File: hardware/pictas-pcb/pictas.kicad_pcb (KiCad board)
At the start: 2 copper layers, 69.8 x 74.9 mm, 27 parts, among them J1 NES_CNT1/2, J10 VizBoard2, J11 VizBoard3, J12 GB, J16 LED_Power_Jack, J2 N64_CNT1/2, J3 N64_CNT3/4, J4 DB1/2, J5 ICSP_VIZ, J6 ICSP_PLAY, J7 USB Port, J8 VizBoard0, J9 VizBoard1, U1 PIC18LF47K42, U2 W25Q128JVS, U3 PIC18F27K42, U4 TPS2115APWR, U5 MCP2221A

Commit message: Revised PCB design again.
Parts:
- added C4: 0.1uF, Capacitor_THT:C_Disc_D3.4mm_W2.1mm_P2.50mm, F.Cu at (125.9, 134.6)
- added C5: 0.1uF, Capacitor_THT:C_Disc_D3.4mm_W2.1mm_P2.50mm, F.Cu at (132.1, 131.7)
- added J13: RCA Input, pictas:PJRAN1X1U04X, F.Cu at (107.4, 134.4)
- added J14: SYNC, Connector_PinHeader_2.54mm:PinHeader_1x03_P2.54mm_Horizontal, F.Cu at (119.9, 130.7)
- added J15: CON_RESET, Connector_PinHeader_2.54mm:PinHeader_1x02_P2.54mm_Horizontal, F.Cu at (83.8, 130.7)
- added Q1: KSC1815_CON_RESET, digikey-footprints:TO-92-3_Formed_Leads, F.Cu at (77.5, 135.9)
- added R7: 680k, Resistor_THT:R_Axial_DIN0204_L3.6mm_D1.6mm_P5.08mm_Horizontal, F.Cu at (133.6, 134.6)
- added SW1: MCU_RESET, Button_Switch_THT:SW_PUSH_6mm_H7.3mm, F.Cu at (125.1, 54.5)
- added U6: LM1881, Package_SO:SOIC-8_3.9x4.9mm_P1.27mm, F.Cu at (126.2, 130.6)
- J10: value VizBoard2 -> VIZ_BOARD_3
- J11: value VizBoard3 -> VIZ_BOARD_4
- J16: value LED_Power_Jack -> LED POWER
- J4: value DB1/2 -> DSUB1/2
- J5, J6: footprint Connector_PinHeader_2.54mm:PinHeader_1x05_P2.54mm_Vertical -> Connector_PinHeader_2.54mm:PinHeader_1x05_P2.54mm_Horizontal
- J8: value VizBoard0 -> VIZ_BOARD_1
- J9: value VizBoard1 -> VIZ_BOARD_2
- moved J5 10.2 mm to (88.4, 61.0), turned to 90 degrees
- moved J6 10.2 mm to (107.3, 61.0), turned to 90 degrees
- moved J7 5.66 mm to (94.5, 123.2)
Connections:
- net /DB11 renamed /DSUB11
- net /DB12 renamed /DSUB12
- net /DB13 renamed /DSUB13
- net /DB14 renamed /DSUB14
- net /DB15 renamed /DSUB15
- net /DB16 renamed /DSUB16
- net /DB17 renamed /DSUB17
- net /DB21 renamed /DSUB21
- net /DB22 renamed /DSUB22
- net /DB23 renamed /DSUB23
- net /DB24 renamed /DSUB24
- net /DB25 renamed /DSUB25
- net /DB26 renamed /DSUB26
- net /DB27 renamed /DSUB27
- J10 pad 2: /STROBE2 -> /STROBE3
- J11 pad 2: /STROBE3 -> /STROBE4
- J5 pad 1: Net-(J5-Pad1) -> GND
- J5 pad 2: Net-(J5-Pad2) -> VDD
- J5 pad 4: VDD -> Net-(J5-Pad4)
- J5 pad 5: GND -> MCU_RESET
- J6 pad 1: Net-(J6-Pad1) -> GND
- J6 pad 2: Net-(J6-Pad2) -> VDD
- J6 pad 4: VDD -> Net-(J6-Pad4)
- J6 pad 5: GND -> MCU_RESET
- J8 pad 2: /STROBE0 -> /STROBE1
- J9 pad 2: /STROBE1 -> /STROBE2
- R5 pad 1: Net-(J6-Pad1) -> MCU_RESET
- R6 pad 2: Net-(J5-Pad1) -> MCU_RESET
- U1 pad 1: Net-(J6-Pad1) -> MCU_RESET
- U1 pad 13: Net-(U1-Pad13) -> ALT_CLK
- U1 pad 20: Net-(U1-Pad20) -> CON_RESET
- U1 pad 21: Net-(U1-Pad21) -> OEOUT
- U1 pad 40: Net-(J6-Pad2) -> Net-(J6-Pad4)
- U3 pad 1: Net-(J5-Pad1) -> MCU_RESET
- U3 pad 28: Net-(J5-Pad2) -> Net-(J5-Pad4)
- U3 pad 4: /STROBE0 -> /STROBE1
- U3 pad 5: /STROBE1 -> /STROBE2
- U3 pad 6: /STROBE2 -> /STROBE3
- U3 pad 7: /STROBE3 -> /STROBE4
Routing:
- net GND: track 305.0 -> 439.5 mm
- net VDD: track 109.7 -> 169.2 mm
- net ALT_CLK: track 0.00 -> 56.0 mm
- net MCU_RESET: track 0.00 -> 49.8 mm
- net CON_RESET: track 0.00 -> 47.6 mm, vias 0 -> 1
- net /STROBE4: track 0.00 -> 42.0 mm
- net OEOUT: track 0.00 -> 34.8 mm, vias 0 -> 2
- net /CVIN: track 0.00 -> 19.5 mm
- net Net-(J5-Pad1): track 19.4 -> 0.00 mm
- net Net-(J6-Pad1): track 18.2 -> 0.00 mm
- net /STROBE3: track 42.0 -> 30.1 mm
- net /STROBE0: track 11.9 -> 0.00 mm
- net Net-(C5-Pad2): track 0.00 -> 10.3 mm
- net /STROBE2: track 30.1 -> 20.4 mm
- net Net-(J5-Pad4): track 0.00 -> 9.42 mm
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- added copper zone on B.Cu, net GND
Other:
- board size 69.8 x 74.9 mm -> 69.8 x 87.5 mm
- board text added: "ALTCLK"
- board text added: "CLK"
- board text added: "CON RESET"
- board text added: "CVIN"
- board text added: "DAT"
- board text added: "GND"
- board text added: "MCU_PLAY"
- board text added: "MCU_VIZ"
- board text added: "OEOUT"
- board text added: "PICTAS Prototype 2021-07-16 Designed by Bigbass"
- board text added: "RESET DEVICE"
- board text added: "VDD"
- board text added: "~MCLR"
- board text removed: "Designed by Bigbass"
- board text removed: "PICTAS Prototype"

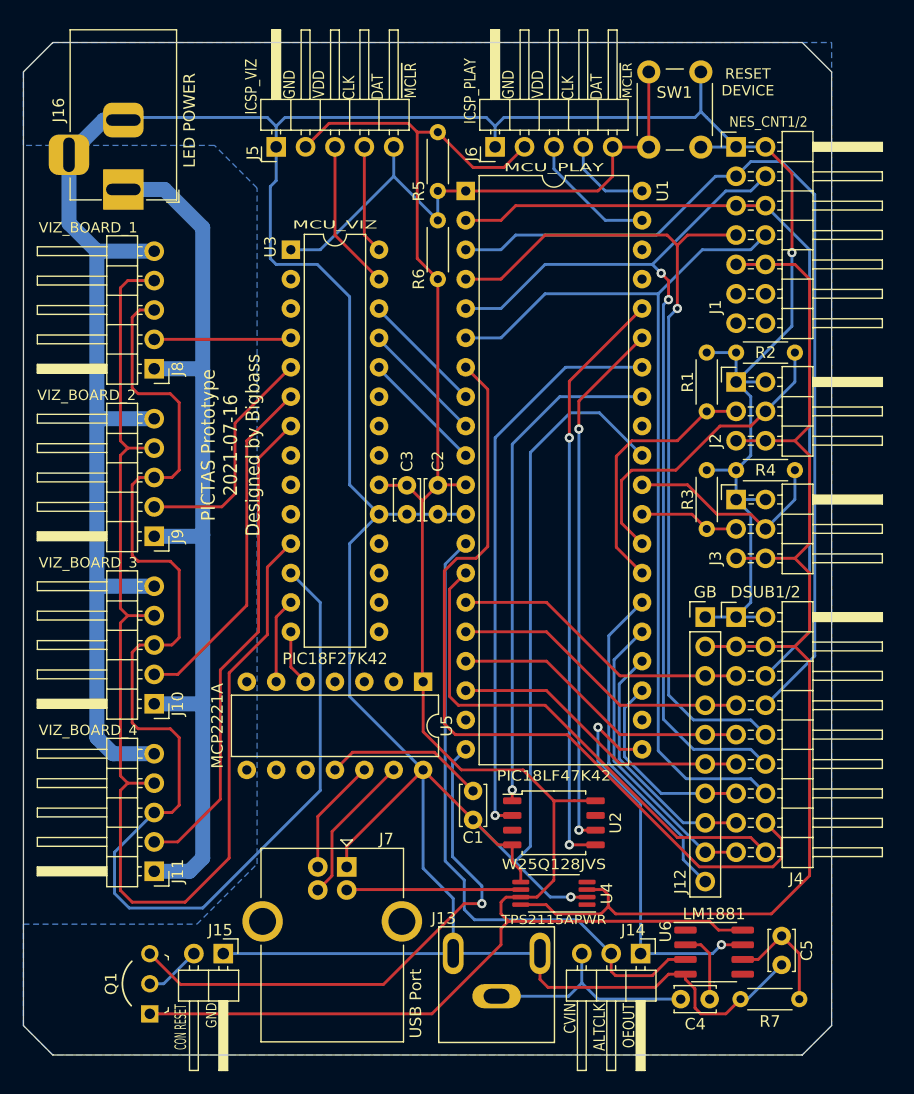
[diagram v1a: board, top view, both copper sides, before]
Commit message: Partially working. SPI to FLASH has severe issues on PCB
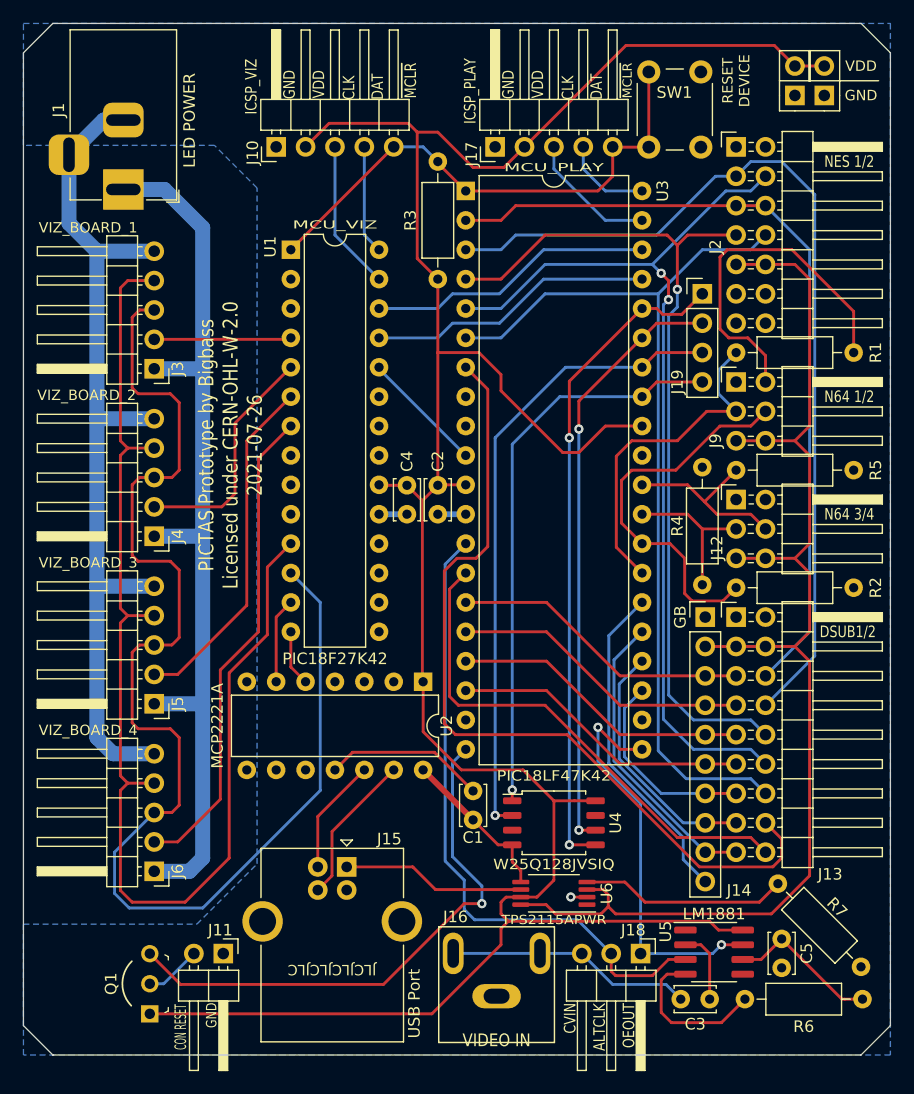
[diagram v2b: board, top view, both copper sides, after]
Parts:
- removed the J13 at (107.4, 134.4)
- removed the R5 at (102.4, 64.8)
- added J15: USB Port, Connector_USB:USB_B_OST_USB-B1HSxx_Horizontal, F.Cu at (94.5, 123.2)
- added J16: VIDEO IN, pictas:PJRAN1X1U04X, F.Cu at (107.4, 134.4)
- added J19: AUX_FLASH, Connector_PinHeader_2.54mm:PinHeader_1x04_P2.54mm_Vertical, F.Cu at (125.2, 73.7)
- added J8: AUX_VDD_GND_2, Connector_PinSocket_2.54mm:PinSocket_1x02_P2.54mm_Vertical, F.Cu at (133.2, 56.5)
- added R7: 400, Resistor_THT:R_Axial_DIN0207_L6.3mm_D2.5mm_P10.16mm_Horizontal, F.Cu at (138.9, 131.8)
- J12: renamed from J3; value N64_CNT3/4 -> N64 3/4
- J2: renamed from J1; value NES_CNT1/2 -> NES 1/2
- J7: value USB Port -> AUX_VDD_GND_1; footprint Connector_USB:USB_B_OST_USB-B1HSxx_Horizontal -> Connector_PinHeader_2.54mm:PinHeader_1x02_P2.54mm_Vertical
- J9: renamed from J2; value N64_CNT1/2 -> N64 1/2
- R1, R2: footprint Resistor_THT:R_Axial_DIN0204_L3.6mm_D1.6mm_P5.08mm_Horizontal -> Resistor_THT:R_Axial_DIN0207_L6.3mm_D2.5mm_P10.16mm_Horizontal
- R3: renamed from R6; footprint Resistor_THT:R_Axial_DIN0204_L3.6mm_D1.6mm_P5.08mm_Horizontal -> Resistor_THT:R_Axial_DIN0207_L6.3mm_D2.5mm_P10.16mm_Horizontal
- R4: renamed from R3; footprint Resistor_THT:R_Axial_DIN0204_L3.6mm_D1.6mm_P5.08mm_Horizontal -> Resistor_THT:R_Axial_DIN0207_L6.3mm_D2.5mm_P10.16mm_Horizontal
- R5: renamed from R4; footprint Resistor_THT:R_Axial_DIN0204_L3.6mm_D1.6mm_P5.08mm_Horizontal -> Resistor_THT:R_Axial_DIN0207_L6.3mm_D2.5mm_P10.16mm_Horizontal
- R6: renamed from R7; footprint Resistor_THT:R_Axial_DIN0204_L3.6mm_D1.6mm_P5.08mm_Horizontal -> Resistor_THT:R_Axial_DIN0207_L6.3mm_D2.5mm_P10.16mm_Horizontal
- U4: renamed from U2; value W25Q128JVS -> W25Q128JVSIQ
- moved J7 78.4 mm to (135.8, 56.5), turned to 180 degrees
- moved R2 22.7 mm to (138.3, 99.1), turned to 180 degrees
- moved R1 12.7 mm to (138.3, 78.7), turned to 180 degrees
- moved R5 10.2 mm to (138.3, 88.9), turned to 180 degrees
- moved R6 5.46 mm to (139.1, 134.6)
- moved R4 0.46 mm to (125.2, 88.6)
- moved C5 0.25 mm to (132.1, 131.9)
- renumbered C4 to C3, C3 to C4, J16 to J1, J5 to J10, J15 to J11, J4 to J13, J12 to J14, J6 to J17, J14 to J18, J8 to J3, J9 to J4, J10 to J5, J11 to J6, U3 to U1, U5 to U2, U1 to U3, U6 to U5, U4 to U6
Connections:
- J7 pad 2: /D+ -> VDD
- U1 pad 25: /UART--> -> UART_V2P
- U1 pad 26: /UART<-- -> UART_P2V
- U1 pad 8: Net-(U3-Pad8) -> GND
- U2 pad 12: /D+ -> /D-
- U2 pad 13: /D- -> /D+
- U3 pad 37: Net-(U1-Pad37) -> UART_V2P
- U3 pad 38: Net-(U1-Pad38) -> UART_P2V
- U3 pad 8: /UART<-- -> Net-(U3-Pad8)
- U3 pad 9: /UART--> -> Net-(U3-Pad9)
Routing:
- net GND: track 439.5 -> 142.2 mm, vias 2 -> 1
- net VDD: track 169.2 -> 222.4 mm
- net UART_P2V: track 0.00 -> 24.8 mm
- net UART_V2P: track 0.00 -> 24.8 mm
- net Net-(R7-Pad2): track 0.00 -> 17.9 mm
- net /UART-->: track 10.7 -> 0.00 mm
- net /UART<--: track 10.7 -> 0.00 mm
- net /N64_DATA1: track 23.0 -> 29.3 mm
- net /N64_DATA2: track 27.2 -> 33.6 mm
- net SPI1SDI: track 51.2 -> 57.4 mm
- net SPI1SDO: track 49.3 -> 55.1 mm
- net SPI1SCK: track 46.2 -> 52.0 mm
- net SPI1CS: track 43.7 -> 49.5 mm
- net /N64_DATA3: track 8.65 -> 13.5 mm
- net MCU_RESET: track 49.8 -> 45.8 mm
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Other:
- board size 69.8 x 87.5 mm -> 74.9 x 89.2 mm
- board text added: "PICTAS Prototype by Bigbass Licensed under CERN-OHL-W-2.0 2021-07-26"
- board text removed: "PICTAS Prototype 2021-07-16 Designed by Bigbass"

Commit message: More redesign progress
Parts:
- added C6: 0.1uF, Capacitor_THT:C_Disc_D3.4mm_W2.1mm_P2.50mm, F.Cu at (106.4, 63.5)
- added JP1: VDD_BYPASS, Jumper:SolderJumper-2_P1.3mm_Open_RoundedPad1.0x1.5mm, F.Cu at (103.4, 127.0)
- moved U4 52.8 mm to (112.4, 66.5)
- moved R7 43.3 mm to (98.0, 117.6), turned to 315 degrees
- moved C1 15.8 mm to (89.7, 119.8)
- moved J19 9.25 mm to (122.7, 82.5)
- moved C2 7.62 mm to (102.6, 100.3)
- moved U3 7.62 mm to (104.9, 72.4)
- moved C5 2.64 mm to (134.6, 131.2), turned to 180 degrees
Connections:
- J19 pad 3: SPI1SDO -> SPI1CS
- J19 pad 4: SPI1CS -> SPI1SDO
- U3 pad 33: SPI1CS -> SPI1SDO
- U3 pad 34: SPI1SDO -> SPI1CS
- U4 pad 3: Net-(U4-Pad3) -> VDD
- U4 pad 7: Net-(U4-Pad7) -> VDD
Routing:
- net GND: track 142.2 -> 87.3 mm, vias 1 -> 4
- net SPI1SDI: track 57.4 -> 23.5 mm, vias 2 -> 0
- net SPI1SCK: track 52.0 -> 26.9 mm, vias 2 -> 0
- net SPI1SDO: track 55.1 -> 33.5 mm, vias 1 -> 0
- net MCU_RESET: track 45.8 -> 62.5 mm, vias 0 -> 2
- net SPI1CS: track 49.5 -> 33.0 mm, vias 1 -> 0
- net /DSUB25: track 79.9 -> 96.2 mm, vias 0 -> 3
- net /CLK: track 114.1 -> 99.2 mm
- net OEOUT: track 34.8 -> 20.3 mm, vias 2 -> 1
- net CON_RESET: track 47.6 -> 33.4 mm, vias 1 -> 2
- net /DSUB24: track 81.1 -> 93.9 mm
- net VDD: track 222.4 -> 233.7 mm
- net /UART_HOST: track 10.7 -> 21.4 mm
- net /GB8: track 28.8 -> 18.7 mm
- net /DSUB23: track 74.7 -> 83.8 mm, vias 1 -> 2
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
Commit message: More design changes
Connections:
- J19 pad 1: SPI1SDI -> SPI1SDO
- J19 pad 4: SPI1SDO -> SPI1SDI
- U3 pad 33: SPI1SDO -> SPI1SDI
- U3 pad 36: SPI1SDI -> SPI1SDO
- U4 pad 2: SPI1SDO -> SPI1SDI
- U4 pad 5: SPI1SDI -> SPI1SDO
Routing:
- net SPI1SDO: track 33.5 -> 23.5 mm
- net SPI1SDI: track 23.5 -> 33.5 mm

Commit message: Finalized new prototype designs.
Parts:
- added C6: 0.1uF, Capacitor_THT:C_Disc_D3.4mm_W2.1mm_P2.50mm, F.Cu at (134.6, 128.7)
- added REF**: OSHW-Logo2_7.3x6mm_SilkScreen, Symbol:OSHW-Logo2_7.3x6mm_SilkScreen, F.Cu at (83.2, 68.6)
- moved C1 2.25 mm to (89.7, 117.6), turned to 0 degrees
- renumbered C6 to C4, C4 to C5, C5 to C7
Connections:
- U1 pad 10: Net-(U1-Pad10) -> unconnected-(U1-Pad10)
- U1 pad 15: Net-(U1-Pad15) -> unconnected-(U1-Pad15)
- U1 pad 16: Net-(U1-Pad16) -> unconnected-(U1-Pad16)
- U1 pad 17: Net-(U1-Pad17) -> unconnected-(U1-Pad17)
- U1 pad 18: Net-(U1-Pad18) -> unconnected-(U1-Pad18)
- U1 pad 2: Net-(U1-Pad2) -> unconnected-(U1-Pad2)
- U1 pad 21: Net-(U1-Pad21) -> unconnected-(U1-Pad21)
- U1 pad 22: Net-(U1-Pad22) -> unconnected-(U1-Pad22)
- U1 pad 23: Net-(U1-Pad23) -> unconnected-(U1-Pad23)
- U1 pad 3: Net-(U1-Pad3) -> unconnected-(U1-Pad3)
- U1 pad 9: Net-(U1-Pad9) -> unconnected-(U1-Pad9)
- U2 pad 10: Net-(U2-Pad10) -> unconnected-(U2-Pad10)
- U2 pad 2: Net-(U2-Pad2) -> unconnected-(U2-Pad2)
- U2 pad 3: Net-(U2-Pad3) -> unconnected-(U2-Pad3)
- U2 pad 4: Net-(U2-Pad4) -> unconnected-(U2-Pad4)
- U2 pad 7: Net-(U2-Pad7) -> unconnected-(U2-Pad7)
- U2 pad 8: Net-(U2-Pad8) -> unconnected-(U2-Pad8)
- U2 pad 9: Net-(U2-Pad9) -> unconnected-(U2-Pad9)
- U3 pad 19: Net-(U3-Pad19) -> unconnected-(U3-Pad19)
- U3 pad 22: Net-(U3-Pad22) -> unconnected-(U3-Pad22)
- U3 pad 8: Net-(U3-Pad8) -> unconnected-(U3-Pad8)
- U3 pad 9: Net-(U3-Pad9) -> unconnected-(U3-Pad9)
- U5 pad 1: Net-(U5-Pad1) -> unconnected-(U5-Pad1)
- U5 pad 5: Net-(U5-Pad5) -> unconnected-(U5-Pad5)
- U6 pad 1: Net-(U6-Pad1) -> unconnected-(U6-Pad1)
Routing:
- net /DSUB26: track 64.1 -> 51.3 mm, vias 1 -> 3
- net /DSUB11: track 23.8 -> 30.4 mm
- net MCU_RESET: track 62.5 -> 68.6 mm, vias 2 -> 1
- net /DSUB12: track 23.8 -> 26.5 mm
- net VDD: track 233.7 -> 236.0 mm
- net /DSUB22: track 83.4 -> 81.4 mm
- net /STROBE3: track 30.1 -> 31.6 mm
- net Net-(C1-Pad2): track 4.86 -> 3.32 mm
- net /USB_5V: track 16.9 -> 18.3 mm
- net /DSUB27: track 40.3 -> 41.7 mm, vias 2 -> 1
- net /DSUB17: track 18.0 -> 19.5 mm
- net /STROBE2: track 20.4 -> 21.8 mm
- net /DSUB21: track 77.4 -> 78.6 mm
- net ALT_CLK: track 51.3 -> 50.4 mm, vias 1 -> 2
- net /GB8: track 18.7 -> 19.6 mm
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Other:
- net class Default removed
- board text added: "PICTAS Prototype by Bigbass Licensed under CERN-OHL-W-2.0 2021-09-21"
- board text added: "~{MCLR}"
- board text removed: "PICTAS Prototype by Bigbass Licensed under CERN-OHL-W-2.0 2021-07-26"
- board text removed: "~MCLR"
